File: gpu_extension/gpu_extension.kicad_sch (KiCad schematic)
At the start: 0 parts

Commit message: schematic for gpu extension
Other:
- sheet Memory ports: added PSRAM{CE# SCLK IO[0..7] RWDS}; removed PSRAM{CE# SCLK SIO[0..3]}
- sheet RP2040 ports: added BUS{RE# SCLK D[0..3] CE#[0..1]}, DVI{CK- CK+ D0- D0+ D1- D1+ D2- D2+ HPD}, PSRAM{CE# SCLK IO[0..7] RWDS}; removed BUS{RE#[0..1] SCLK D[0..3] CE#[0..1]}, DVI{CK- CK+ D0- D0+ D1- D1+ D2- D2+ SDA SCL CEC}, PSRAM{CE# SCLK SIO[0..3]}
- sheet Video Output ports: added DVI{CK- CK+ D0- D0+ D1- D1+ D2- D2+ HPD}; removed DVI{CK- CK+ D0- D0+ D1- D1+ D2- D2+ SDA SCL CEC}

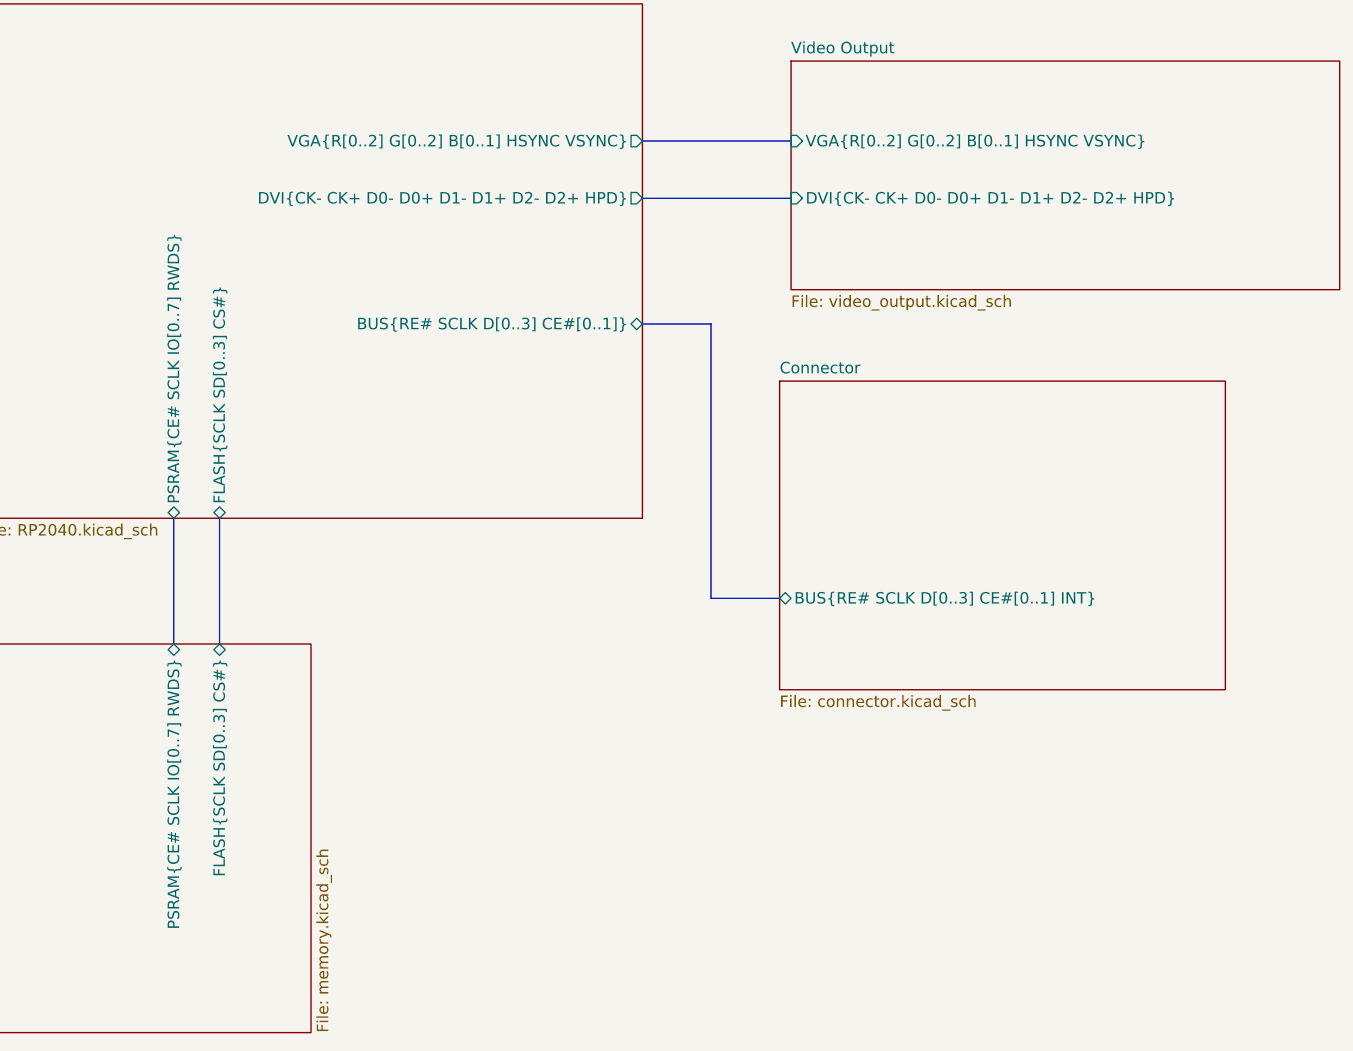
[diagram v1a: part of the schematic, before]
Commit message: some ERC fixes
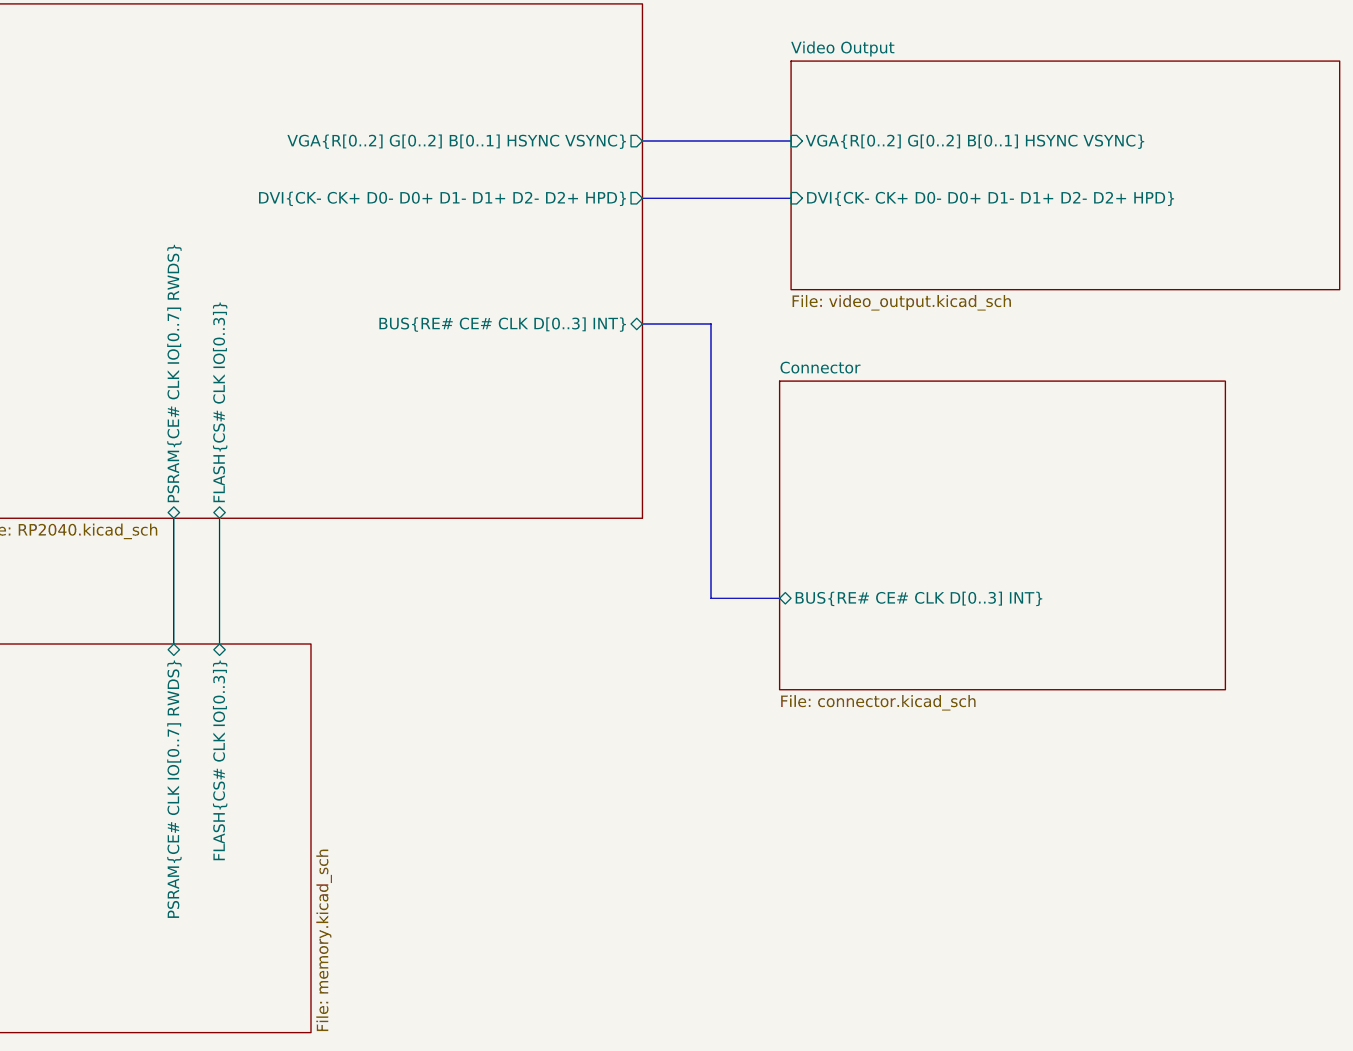
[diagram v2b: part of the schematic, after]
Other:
- sheet Connector ports: added BUS{RE# CE# CLK D[0..3] INT}; removed BUS{RE# SCLK D[0..3] CE#[0..1] INT}
- sheet Memory ports: added FLASH{CS# CLK IO[0..3]}, PSRAM{CE# CLK IO[0..7] RWDS}; removed FLASH{SCLK SD[0..3] CS#}, PSRAM{CE# SCLK IO[0..7] RWDS}
- sheet RP2040 ports: added BUS{RE# CE# CLK D[0..3] INT}, FLASH{CS# CLK IO[0..3]}, PSRAM{CE# CLK IO[0..7] RWDS}; removed BUS{RE# SCLK D[0..3] CE#[0..1]}, FLASH{SCLK SD[0..3] CS#}, PSRAM{CE# SCLK IO[0..7] RWDS}
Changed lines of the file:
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@@
       (effects (font (size 1.27 1.27)) (justify left top))
     )
-    (pin "BUS{RE# SCLK D[0..3] CE#[0..1] INT}" bidirectional (at 147.32 120.65 180)
+    (pin "BUS{RE# CE# CLK D[0..3] INT}" bidirectional (at 147.32 120.65 180)
       (effects (font (size 1.27 1.27)) (justify left))
     )
@@
       (effects (font (size 1.27 1.27)) (justify left top))
     )
-    (pin "PSRAM{CE# SCLK IO[0..7] RWDS}" bidirectional (at 80.01 125.73 90)
+    (pin "PSRAM{CE# CLK IO[0..7] RWDS}" bidirectional (at 80.01 125.73 90)
       (effects (font (size 1.27 1.27)) (justify right))
     )
-    (pin "FLASH{SCLK SD[0..3] CS#}" bidirectional (at 85.09 125.73 90)
+    (pin "FLASH{CS# CLK IO[0..3]}" bidirectional (at 85.09 125.73 90)
       (effects (font (size 1.27 1.27)) (justify right))
     )
@@
       (effects (font (size 1.27 1.27)) (justify left top))
     )
-    (pin "FLASH{SCLK SD[0..3] CS#}" bidirectional (at 85.09 111.76 270)
+    (pin "FLASH{CS# CLK IO[0..3]}" bidirectional (at 85.09 111.76 270)
       (effects (font (size 1.27 1.27)) (justify left))
     )
@@
       (effects (font (size 1.27 1.27)) (justify right))
     )
-    (pin "BUS{RE# SCLK D[0..3] CE#[0..1]}" bidirectional (at 132.08 90.17 0)
+    (pin "BUS{RE# CE# CLK D[0..3] INT}" bidirectional (at 132.08 90.17 0)
       (effects (font (size 1.27 1.27)) (justify right))
     )
-    (pin "PSRAM{CE# SCLK IO[0..7] RWDS}" bidirectional (at 80.01 111.76 270)
+    (pin "PSRAM{CE# CLK IO[0..7] RWDS}" bidirectional (at 80.01 111.76 270)
       (effects (font (size 1.27 1.27)) (justify left))
     )

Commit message: refactored mainboard schematic
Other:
- sheet RP2040 ports: added DVI{CK- CK+ D0- D0+ D1- D1+ D2- D2+}; removed DVI{CK- CK+ D0- D0+ D1- D1+ D2- D2+ HPD}, VGA{R[0..2] G[0..2] B[0..1] HSYNC VSYNC}
- sheet Video Output ports: added DVI{CK- CK+ D0- D0+ D1- D1+ D2- D2+}; removed DVI{CK- CK+ D0- D0+ D1- D1+ D2- D2+ HPD}, VGA{R[0..2] G[0..2] B[0..1] HSYNC VSYNC}
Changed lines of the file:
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@@
-    (stroke (width 0) (type default))
-  )
-  (bus (pts (xy 132.08 69.85) (xy 148.59 69.85))
     (stroke (width 0) (type default))
   )
@@
       (effects (font (size 1.27 1.27)) (justify left top))
     )
-    (pin "VGA{R[0..2] G[0..2] B[0..1] HSYNC VSYNC}" input (at 148.59 69.85 180)
-      (effects (font (size 1.27 1.27)) (justify left))
-    )
-    (pin "DVI{CK- CK+ D0- D0+ D1- D1+ D2- D2+ HPD}" input (at 148.59 76.2 180)
+    (pin "DVI{CK- CK+ D0- D0+ D1- D1+ D2- D2+}" input (at 148.59 76.2 180)
       (effects (font (size 1.27 1.27)) (justify left))
     )
@@
       (effects (font (size 1.27 1.27)) (justify left top))
     )
-    (pin "DVI{CK- CK+ D0- D0+ D1- D1+ D2- D2+ HPD}" output (at 132.08 76.2 0)
+    (pin "DVI{CK- CK+ D0- D0+ D1- D1+ D2- D2+}" output (at 132.08 76.2 0)
       (effects (font (size 1.27 1.27)) (justify right))
     )
-    (pin "VGA{R[0..2] G[0..2] B[0..1] HSYNC VSYNC}" output (at 132.08 69.85 0)
-      (effects (font (size 1.27 1.27)) (justify right))
-    )

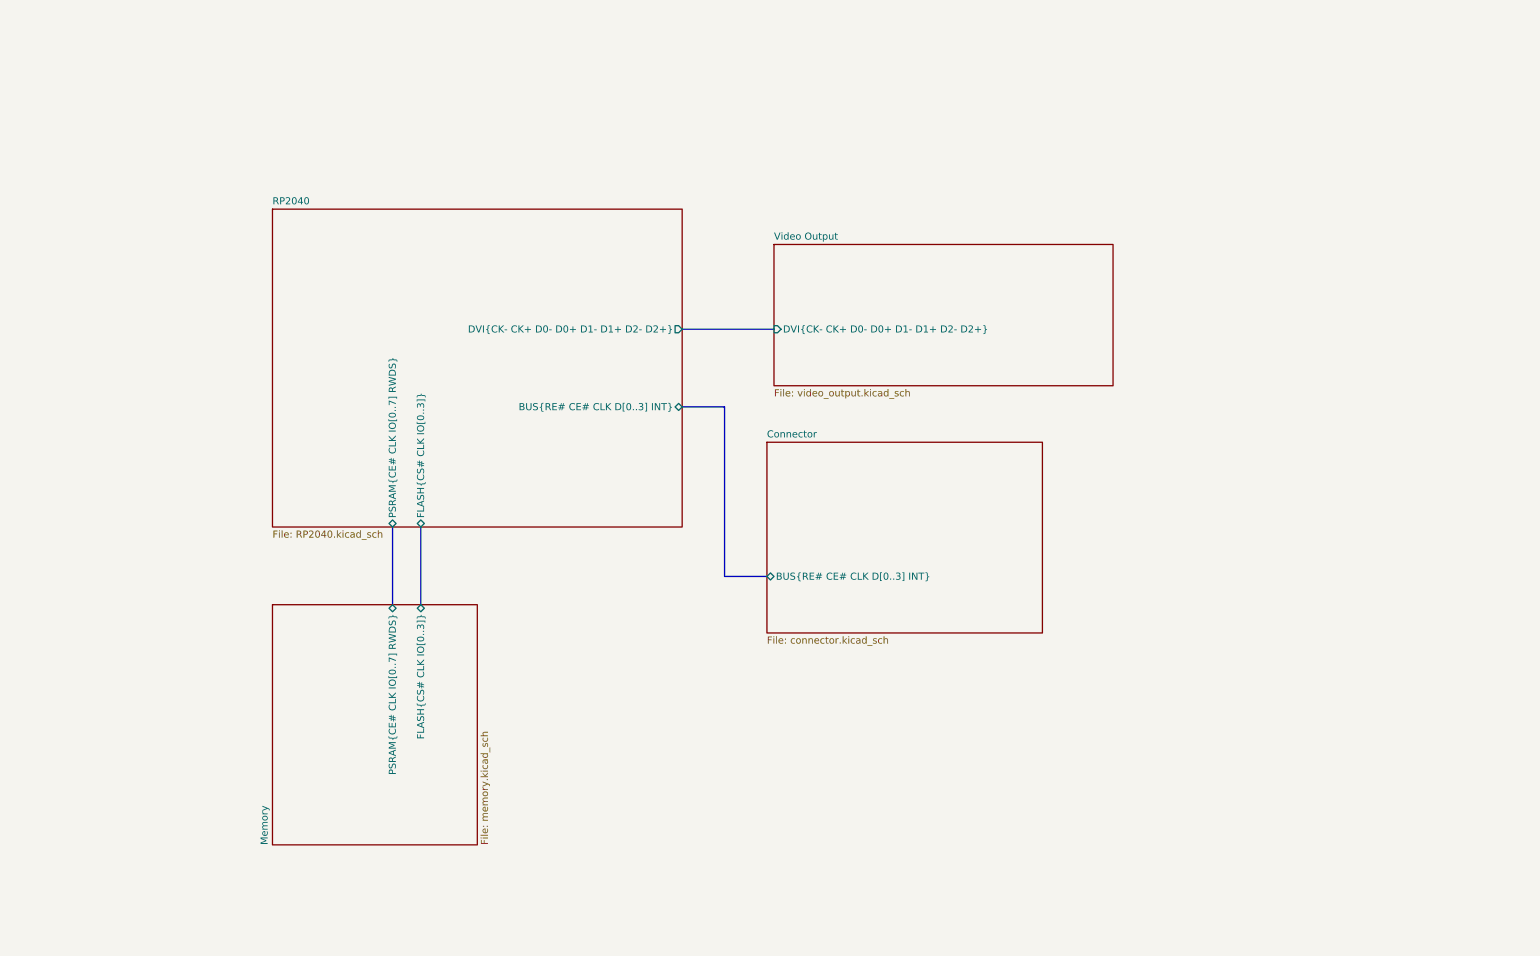
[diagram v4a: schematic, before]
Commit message: fixes in gpu extension schematic
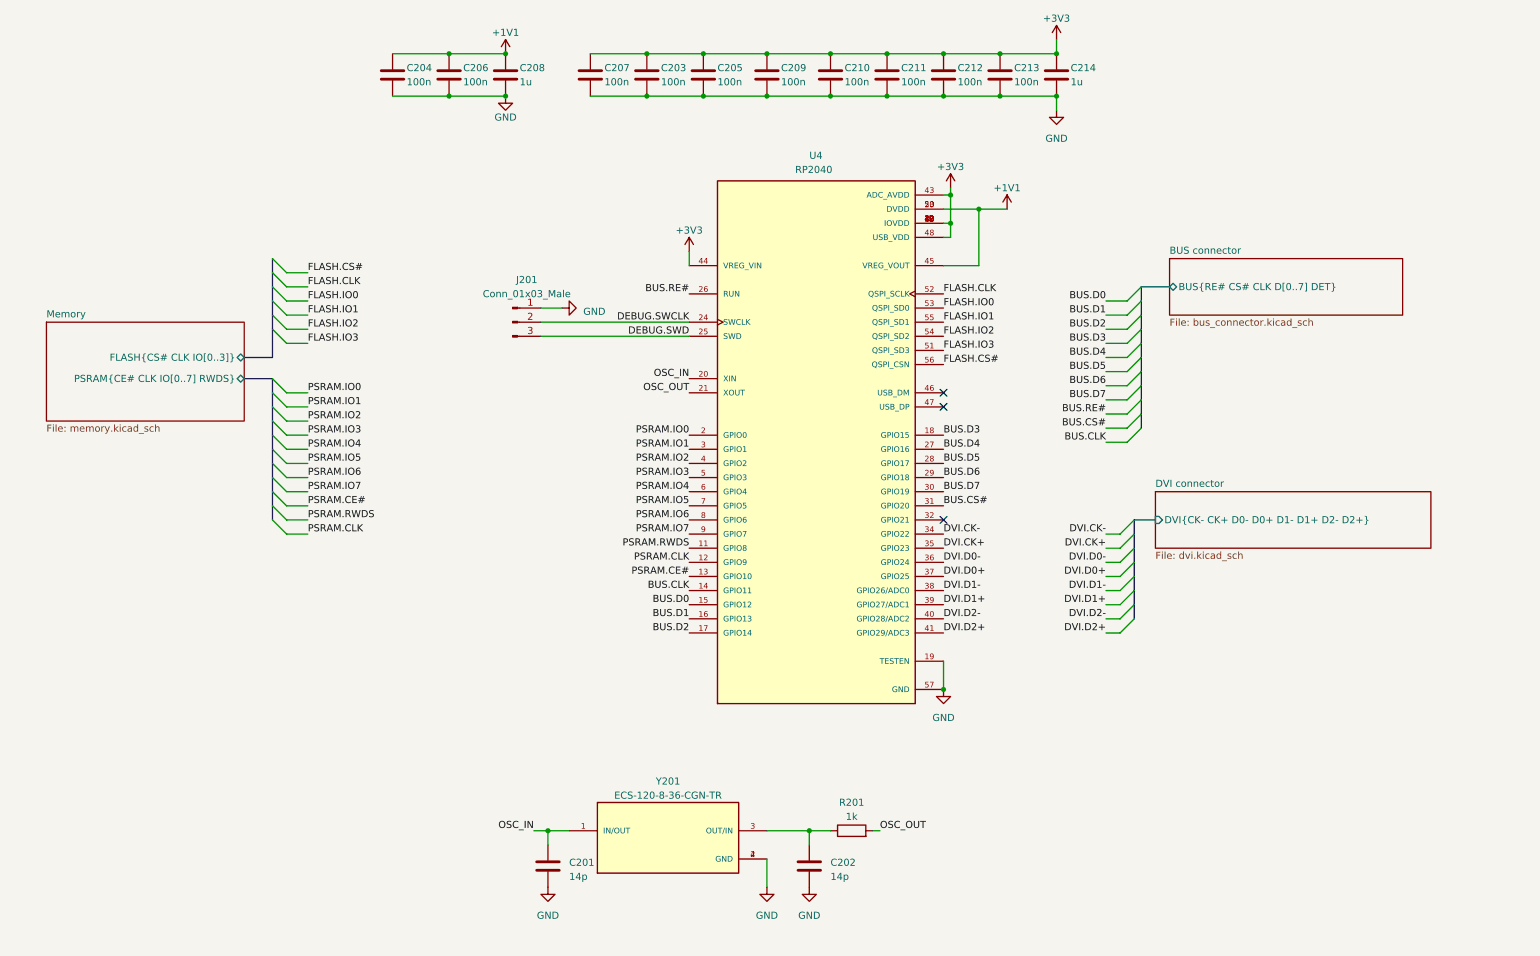
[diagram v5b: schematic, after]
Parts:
- added C201, C202: 14p, Capacitor_SMD:C_0603_1608Metric_Pad1.08x0.95mm_HandSolder, symbol Device:C
- added C203, C204, C205, C206, C207, C209, C210, C211, C212, C213: 100n, Capacitor_SMD:C_0603_1608Metric_Pad1.08x0.95mm_HandSolder, symbol Device:C
- added C208, C214: 1u, Capacitor_SMD:C_0603_1608Metric_Pad1.08x0.95mm_HandSolder, symbol Device:C
- added J201: Conn_01x03_Male, Connector_PinHeader_2.54mm:PinHeader_1x03_P2.54mm_Vertical, symbol Connector:Conn_01x03_Male
- added R201: 1k, Resistor_SMD:R_0603_1608Metric_Pad0.98x0.95mm_HandSolder, symbol Device:R
- added U4: RP2040, QFN40P700X700X90-57N, symbol RP2040:RP2040
- added Y201: ECS-120-8-36-CGN-TR, footprints:XTAL_ECS-120-8-36-CGN-TR, symbol ECS-120-8-36-CGN-TR:ECS-120-8-36-CGN-TR
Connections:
- new net: C202.1, R201.1, Y201.3 (OUT/IN)
- new net +1V1: C204.1, C206.1, C208.1, U4.23 (DVDD), U4.45 (VREG_VOUT), U4.50 (DVDD)
- new net +3V3: C203.1, C205.1, C207.1, C209.1, C210.1, C211.1, C212.1, C213.1, C214.1, U4.1 (IOVDD), U4.10 (IOVDD), U4.22 (IOVDD), U4.33 (IOVDD), U4.42 (IOVDD), U4.43 (ADC_AVDD), U4.44 (VREG_VIN), U4.48 (USB_VDD), U4.49 (IOVDD)
- new net BUS.CLK: U4.14 (GPIO11)
- new net BUS.CS#: U4.31 (GPIO20)
- new net BUS.D0: U4.15 (GPIO12)
- new net BUS.D1: U4.16 (GPIO13)
- new net BUS.D2: U4.17 (GPIO14)
- new net BUS.D3: U4.18 (GPIO15)
- new net BUS.D4: U4.27 (GPIO16)
- new net BUS.D5: U4.28 (GPIO17)
- new net BUS.D6: U4.29 (GPIO18)
- new net BUS.D7: U4.30 (GPIO19)
- new net BUS.RE#: U4.26 (RUN)
- new net DEBUG.SWCLK: J201.2 (Pin_2), U4.24 (SWCLK)
- new net DEBUG.SWD: J201.3 (Pin_3), U4.25 (SWD)
- new net DVI.CK+: U4.35 (GPIO23)
- new net DVI.CK-: U4.34 (GPIO22)
- new net DVI.D0+: U4.37 (GPIO25)
- new net DVI.D0-: U4.36 (GPIO24)
- new net DVI.D1+: U4.39 (GPIO27/ADC1)
- new net DVI.D1-: U4.38 (GPIO26/ADC0)
- new net DVI.D2+: U4.41 (GPIO29/ADC3)
- new net DVI.D2-: U4.40 (GPIO28/ADC2)
- new net FLASH.CLK: U4.52 (QSPI_SCLK)
- new net FLASH.CS#: U4.56 (QSPI_CSN)
- new net FLASH.IO0: U4.53 (QSPI_SD0)
- new net FLASH.IO1: U4.55 (QSPI_SD1)
- new net FLASH.IO2: U4.54 (QSPI_SD2)
- new net FLASH.IO3: U4.51 (QSPI_SD3)
- new net GND: C201.2, C202.2, C203.2, C204.2, C205.2, C206.2, C207.2, C208.2, C209.2, C210.2, C211.2, C212.2, C213.2, C214.2, J201.1 (Pin_1), U4.19 (TESTEN), U4.57 (GND), Y201.2 (GND), Y201.4 (GND)
- new net OSC_IN: C201.1, U4.20 (XIN), Y201.1 (IN/OUT)
- new net OSC_OUT: R201.2, U4.21 (XOUT)
- new net PSRAM.CE#: U4.13 (GPIO10)
- new net PSRAM.CLK: U4.12 (GPIO9)
- new net PSRAM.IO0: U4.2 (GPIO0)
- new net PSRAM.IO1: U4.3 (GPIO1)
- new net PSRAM.IO2: U4.4 (GPIO2)
- new net PSRAM.IO3: U4.5 (GPIO3)
- new net PSRAM.IO4: U4.6 (GPIO4)
- new net PSRAM.IO5: U4.7 (GPIO5)
- new net PSRAM.IO6: U4.8 (GPIO6)
- new net PSRAM.IO7: U4.9 (GPIO7)
- new net PSRAM.RWDS: U4.11 (GPIO8)
- no-connect marks 0 -> 3
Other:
- removed sheet Connector
- removed sheet RP2040
- removed sheet Video Output
- added sheet BUS connector (bus_connector.kicad_sch)
- added sheet DVI connector (dvi.kicad_sch)

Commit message: fixes
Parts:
- C201, C202, C203, C204, C205, C206, C207, C208, C209, C210, C211, C212, C213, C214: footprint Capacitor_SMD:C_0603_1608Metric_Pad1.08x0.95mm_HandSolder -> Capacitor_SMD:C_0402_1005Metric_Pad0.74x0.62mm_HandSolder
- R201: footprint Resistor_SMD:R_0603_1608Metric_Pad0.98x0.95mm_HandSolder -> Resistor_SMD:R_0402_1005Metric_Pad0.72x0.64mm_HandSolder
- U4: footprint QFN40P700X700X90-57N -> footprints:QFN40P700X700X90-57N
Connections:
- net BUS.CLK is gone; now on net DVI.D0+: U4.14 (GPIO11)
- net BUS.D0 is gone; now on net DVI.D1-: U4.15 (GPIO12)
- net BUS.D1 is gone; now on net DVI.D1+: U4.16 (GPIO13)
- net BUS.D2 is gone; now on net DVI.D2-: U4.17 (GPIO14)
- net BUS.D3 is gone; now on net DVI.D2+: U4.18 (GPIO15)
- net PSRAM.CE# is gone; now on net DVI.D0-: U4.13 (GPIO10)
- net PSRAM.CLK is gone; now on net DVI.CK+: U4.12 (GPIO9)
- net PSRAM.RWDS is gone; now on net DVI.CK-: U4.11 (GPIO8)
- net DVI.CK+: no longer U4.35 (GPIO23)
- net DVI.CK-: no longer U4.34 (GPIO22)
- net DVI.D0+: no longer U4.37 (GPIO25)
- net DVI.D0-: no longer U4.36 (GPIO24)
- net DVI.D1+: no longer U4.39 (GPIO27/ADC1)
- net DVI.D1-: no longer U4.38 (GPIO26/ADC0)
- net DVI.D2+: no longer U4.41 (GPIO29/ADC3)
- net DVI.D2-: no longer U4.40 (GPIO28/ADC2)
- net OUT_BUS.D5: now reaches U4.32 (GPIO21)
- net BUS.CS# renamed OUT_BUS.D6
- net BUS.D4 renamed MCU_I2C.DATA
- net BUS.D5 renamed MCU_I2C.CLOCK
- net BUS.D6 renamed OUT_BUS.CLK
- net BUS.D7 renamed OUT_BUS.D7
- net BUS.RE# renamed Render Engine/BUS.RE#
- net FLASH.IO2: no longer names the net of U4.54 (QSPI_SD2)
- net FLASH.IO3: no longer names the net of U4.51 (QSPI_SD3)
- net PSRAM.IO0 renamed VGA.R0
- net PSRAM.IO1 renamed VGA.R1
- net PSRAM.IO2 renamed VGA.R2
- net PSRAM.IO3 renamed VGA.G0
- net PSRAM.IO4 renamed VGA.G1
- net PSRAM.IO5 renamed VGA.G2
- net PSRAM.IO6 renamed VGA.B0
- net PSRAM.IO7 renamed VGA.B1
- new net OUT_BUS.D0: U4.38 (GPIO26/ADC0)
- new net OUT_BUS.D1: U4.37 (GPIO25)
- new net OUT_BUS.D2: U4.36 (GPIO24)
- new net OUT_BUS.D3: U4.35 (GPIO23)
- new net OUT_BUS.D4: U4.34 (GPIO22)
- new net VGA.HSYNC: U4.41 (GPIO29/ADC3)
- new net VGA.VSYNC: U4.40 (GPIO28/ADC2)
- no-connect marks 3 -> 5
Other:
- removed sheet BUS connector
- added sheet Render Engine (render.kicad_sch)
- sheet DVI connector ports: added MCU_I2C{CLOCK DATA}, VGA{R[0..2] G[0..2] B[0..1] HSYNC VSYNC}; removed none
- sheet Memory ports: added FLASH{CS# CLK IO[0..1]}; removed FLASH{CS# CLK IO[0..3]}, PSRAM{CE# CLK IO[0..7] RWDS}
